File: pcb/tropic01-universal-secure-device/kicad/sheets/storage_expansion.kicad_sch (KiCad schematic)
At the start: 0 parts

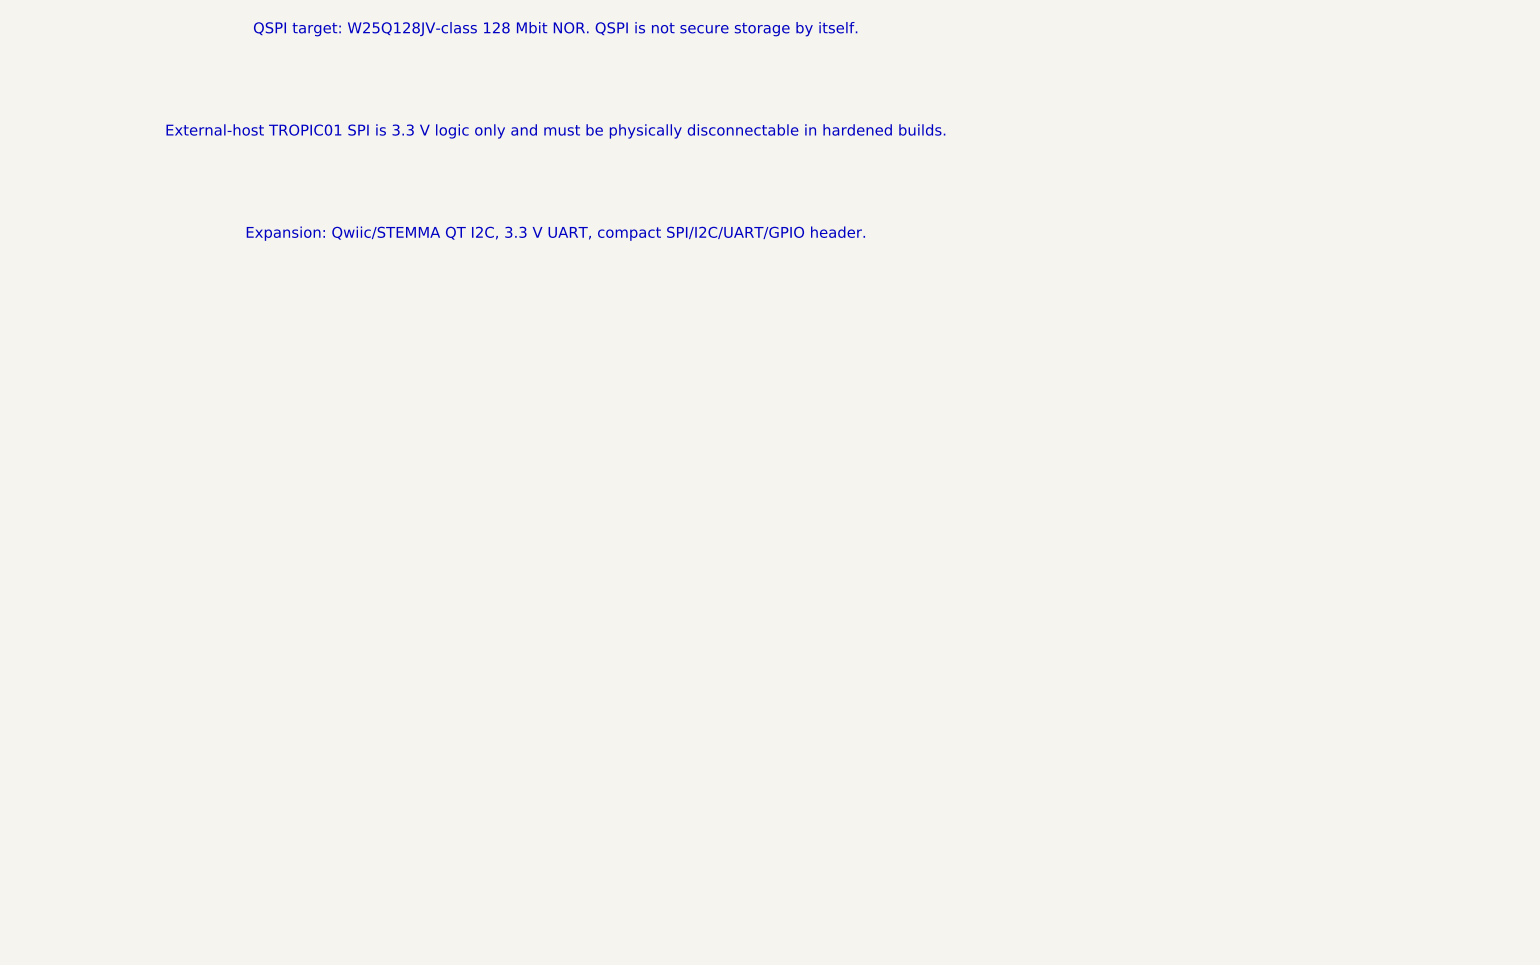
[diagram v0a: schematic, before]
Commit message: feat: materialize tropic01 schematic bindings
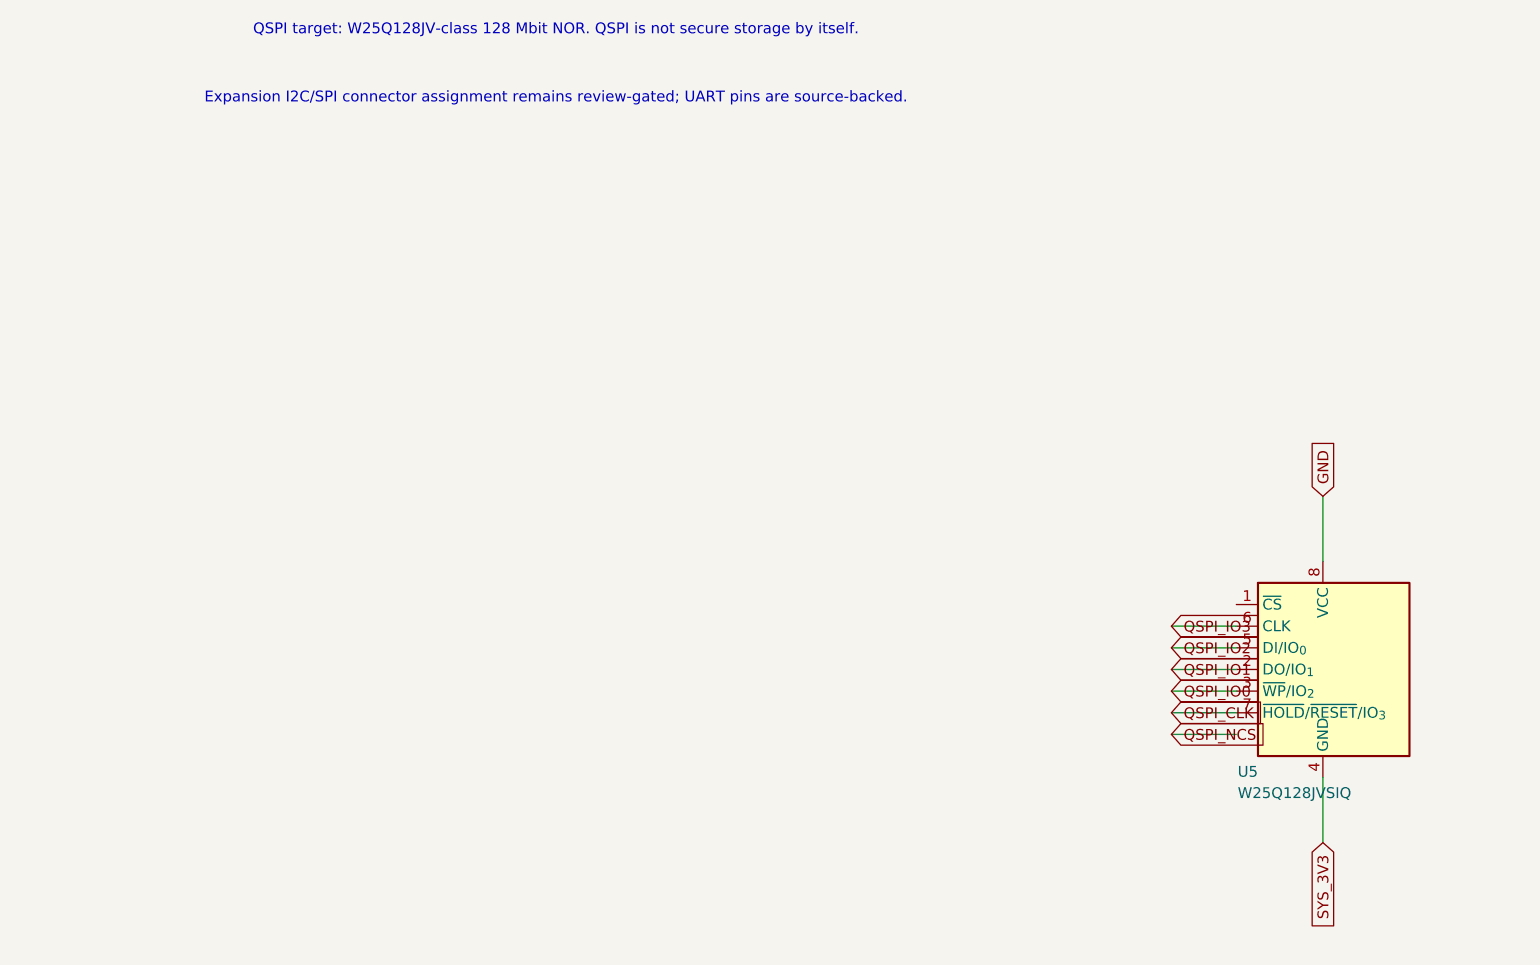
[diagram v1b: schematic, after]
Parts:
- added U5: W25Q128JVSIQ, Package_SO:SOIC-8_5.3x5.3mm_P1.27mm, symbol Memory_Flash:W25Q32JVSS
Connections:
- new net GND: U5.8 (VCC)
- new net QSPI_CLK: U5.7 (~{HOLD}/~{RESET}/IO_{3})
- new net QSPI_IO0: U5.3 (~{WP}/IO_{2})
- new net QSPI_IO1: U5.2 (DO/IO_{1})
- new net QSPI_IO2: U5.5 (DI/IO_{0})
- new net QSPI_IO3: U5.6 (CLK)
- new net SYS_3V3: U5.4 (GND)
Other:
- note added: "Expansion I2C/SPI connector assignment remains review-gated; UART pins are source-backed."
- note removed: "Expansion: Qwiic/STEMMA QT I2C, 3.3 V UART, compact SPI/I2C/UART/GPIO header."
- note removed: "External-host TROPIC01 SPI is 3.3 V logic only and must be physically disconnectable in hardened builds."
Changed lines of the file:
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@@
 	(text "QSPI target: W25Q128JV-class 128 Mbit NOR. QSPI is not secure storage by itself."
 		(exclude_from_sim no)
-		(at 20 20 0)
-		(effects
-			(font
-				(size 1.27 1.27)
+		(at 20.00 20.00 0)
+		(effects (font (size 1.27 1.27)))
+	)
+	(text "Expansion I2C/SPI connector assignment remains review-gated; UART pins are source-backed."
+		(exclude_from_sim no)
+		(at 20.00 28.00 0)
+		(effects (font (size 1.27 1.27)))
+	)
+	(symbol
+		(lib_id "Memory_Flash:W25Q32JVSS")
+		(at 110.00 95.00 0)
+		(unit 1)
+		(exclude_from_sim no)
+		(in_bom yes)
+		(on_board yes)
+		(dnp no)
+		(property "Reference" "U5"
+			(at 100.00 107.00 0)
+			(effects (font (size 1.27 1.27)) (justify left))
+		)
+		(property "Value" "W25Q128JVSIQ"
+			(at 100.00 109.50 0)
+			(effects (font (size 1.27 1.27)) (justify left))
+		)
+		(property "Footprint" "Package_SO:SOIC-8_5.3x5.3mm_P1.27mm"
+			(at 110.00 95.00 0)
+			(effects (font (size 1.27 1.27)) (hide yes))
+		)
+		(property "Datasheet" "https://www.winbond.com/resource-files/w25q128jv_dtr%20revc%2003272018%20plus.pdf"
+			(at 110.00 95.00 0)
+			(effects (font (size 1.27 1.27)) (hide yes))
+		)
+		(property "Description" "128 Mbit SPI/QSPI NOR flash using the KiCad W25Q32JVSS pin-compatible symbol"
+			(at 110.00 95.00 0)
+			(effects (font (size 1.27 1.27)) (hide yes))
+		)
+		(instances
+			(project "tropic01-universal-secure-device"
+				(path "/11111111-1111-4111-8111-111111111111/66666666-6666-4666-8666-666666666666"
+					(reference "U5")
+					(unit 1)
+				)
 			)
 		)
 	)
-	(text "External-host TROPIC01 SPI is 3.3 V logic only and must be physically disconnectable in hardened builds."
-		(exclude_from_sim no)
-		(at 20 32 0)
-		(effects
-			(font
-				(size 1.27 1.27)
-			)
+	(wire
+		(pts
+			(xy 99.84 102.62) (xy 92.22 102.62)
 		)
+		(stroke (width 0) (type default))
 	)
-	(text "Expansion: Qwiic/STEMMA QT I2C, 3.3 V UART, compact SPI/I2C/UART/GPIO header."
-		(exclude_from_sim no)
-		(at 20 44 0)
-		(effects
-			(font
-				(size 1.27 1.27)
-			)
+	(global_label "QSPI_NCS"
+		(shape input)
+		(at 92.22 102.62 0)
+		(fields_autoplaced)
+		(effects (font (size 1.27 1.27)))
+	)
+	(wire
+		(pts
+			(xy 99.84 95.00) (xy 92.22 95.00)
 		)
+		(stroke (width 0) (type default))
+	)
+	(global_label "QSPI_IO1"
+		(shape input)
+		(at 92.22 95.00 0)
+		(fields_autoplaced)
+		(effects (font (size 1.27 1.27)))
+	)
+	(wire
+		(pts
+			(xy 99.84 92.46) (xy 92.22 92.46)
+		)
+		(stroke (width 0) (type default))
+	)
+	(global_label "QSPI_IO2"
+		(shape input)
+		(at 92.22 92.46 0)
+		(fields_autoplaced)
+		(effects (font (size 1.27 1.27)))
+	)
+	(wire
+		(pts
+			(xy 110.00 82.30) (xy 110.00 74.68)
+		)
+		(stroke (width 0) (type default))
+	)
+	(global_label "GND"
+		(shape input)
+		(at 110.00 74.68 90)
+		(fields_autoplaced)
+		(effects (font (size 1.27 1.27)))
+	)
+	(wire
+		(pts
+			(xy 99.84 97.54) (xy 92.22 97.54)
+		)
+		(stroke (width 0) (type default))
+	)
+	(global_label "QSPI_IO0"
+		(shape input)
+		(at 92.22 97.54 0)
+		(fields_autoplaced)
+		(effects (font (size 1.27 1.27)))
+	)
+	(wire
+		(pts
+			(xy 99.84 100.08) (xy 92.22 100.08)
+		)
+		(stroke (width 0) (type default))
+	)
+	(global_label "QSPI_CLK"
+		(shape input)
+		(at 92.22 100.08 0)
+		(fields_autoplaced)
+		(effects (font (size 1.27 1.27)))
+	)
+	(wire
+		(pts
+			(xy 99.84 89.92) (xy 92.22 89.92)
+		)
+		(stroke (width 0) (type default))
+	)
+	(global_label "QSPI_IO3"
+		(shape input)
+		(at 92.22 89.92 0)
+		(fields_autoplaced)
+		(effects (font (size 1.27 1.27)))
+	)
+	(wire
+		(pts
+			(xy 110.00 107.70) (xy 110.00 115.32)
+		)
+		(stroke (width 0) (type default))
+	)
+	(global_label "SYS_3V3"
+		(shape input)
+		(at 110.00 115.32 270)
+		(fields_autoplaced)
+		(effects (font (size 1.27 1.27)))
 	)
 	(sheet_instances

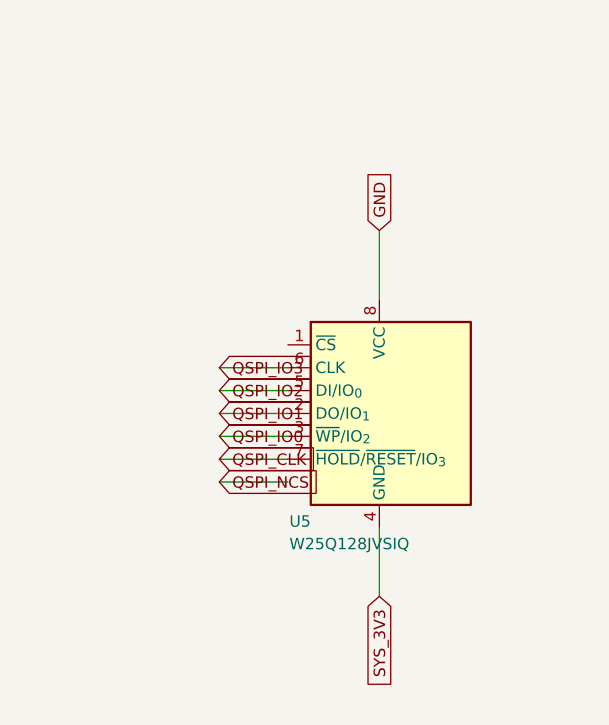
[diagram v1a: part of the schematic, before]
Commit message: feat: bind tropic01 pcb nets
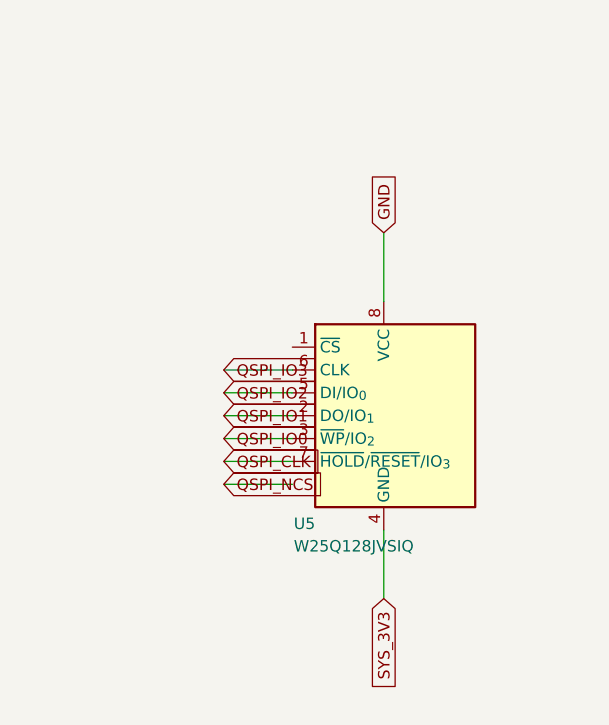
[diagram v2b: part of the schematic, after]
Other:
- moved on the sheet: U5
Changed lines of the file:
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@@
 	(symbol
 		(lib_id "Memory_Flash:W25Q32JVSS")
-		(at 110.00 95.00 0)
+		(at 110.49 95.25 0)
 		(unit 1)
 		(exclude_from_sim no)
@@
 		(dnp no)
 		(property "Reference" "U5"
-			(at 100.00 107.00 0)
+			(at 100.49 107.25 0)
 			(effects (font (size 1.27 1.27)) (justify left))
 		)
 		(property "Value" "W25Q128JVSIQ"
-			(at 100.00 109.50 0)
+			(at 100.49 109.75 0)
 			(effects (font (size 1.27 1.27)) (justify left))
 		)
 		(property "Footprint" "Package_SO:SOIC-8_5.3x5.3mm_P1.27mm"
-			(at 110.00 95.00 0)
+			(at 110.49 95.25 0)
 			(effects (font (size 1.27 1.27)) (hide yes))
 		)
 		(property "Datasheet" "https://www.winbond.com/resource-files/w25q128jv_dtr%20revc%2003272018%20plus.pdf"
-			(at 110.00 95.00 0)
+			(at 110.49 95.25 0)
 			(effects (font (size 1.27 1.27)) (hide yes))
 		)
 		(property "Description" "128 Mbit SPI/QSPI NOR flash using the KiCad W25Q32JVSS pin-compatible symbol"
-			(at 110.00 95.00 0)
+			(at 110.49 95.25 0)
 			(effects (font (size 1.27 1.27)) (hide yes))
 		)
@@
 	(wire
 		(pts
-			(xy 99.84 102.62) (xy 92.22 102.62)
+			(xy 100.33 102.87) (xy 92.71 102.87)
 		)
 		(stroke (width 0) (type default))
@@
 	(global_label "QSPI_NCS"
 		(shape input)
-		(at 92.22 102.62 0)
+		(at 92.71 102.87 0)
 		(fields_autoplaced)
 		(effects (font (size 1.27 1.27)))
@@
 	(wire
 		(pts
-			(xy 99.84 95.00) (xy 92.22 95.00)
+			(xy 100.33 95.25) (xy 92.71 95.25)
 		)
 		(stroke (width 0) (type default))
@@
 	(global_label "QSPI_IO1"
 		(shape input)
-		(at 92.22 95.00 0)
+		(at 92.71 95.25 0)
 		(fields_autoplaced)
 		(effects (font (size 1.27 1.27)))
@@
 	(wire
 		(pts
-			(xy 99.84 92.46) (xy 92.22 92.46)
+			(xy 100.33 92.71) (xy 92.71 92.71)
 		)
 		(stroke (width 0) (type default))
@@
 	(global_label "QSPI_IO2"
 		(shape input)
-		(at 92.22 92.46 0)
+		(at 92.71 92.71 0)
 		(fields_autoplaced)
 		(effects (font (size 1.27 1.27)))
@@
 	(wire
 		(pts
-			(xy 110.00 82.30) (xy 110.00 74.68)
+			(xy 110.49 82.55) (xy 110.49 74.93)
 		)
 		(stroke (width 0) (type default))
@@
 	(global_label "GND"
 		(shape input)
-		(at 110.00 74.68 90)
+		(at 110.49 74.93 90)
 		(fields_autoplaced)
 		(effects (font (size 1.27 1.27)))
@@
 	(wire
 		(pts
-			(xy 99.84 97.54) (xy 92.22 97.54)
+			(xy 100.33 97.79) (xy 92.71 97.79)
 		)
 		(stroke (width 0) (type default))
@@
 	(global_label "QSPI_IO0"
 		(shape input)
-		(at 92.22 97.54 0)
+		(at 92.71 97.79 0)
 		(fields_autoplaced)
 		(effects (font (size 1.27 1.27)))
@@
 	(wire
 		(pts
-			(xy 99.84 100.08) (xy 92.22 100.08)
+			(xy 100.33 100.33) (xy 92.71 100.33)
 		)
 		(stroke (width 0) (type default))
@@
 	(global_label "QSPI_CLK"
 		(shape input)
-		(at 92.22 100.08 0)
+		(at 92.71 100.33 0)
 		(fields_autoplaced)
 		(effects (font (size 1.27 1.27)))
@@
 	(wire
 		(pts
-			(xy 99.84 89.92) (xy 92.22 89.92)
+			(xy 100.33 90.17) (xy 92.71 90.17)
 		)
 		(stroke (width 0) (type default))
@@
 	(global_label "QSPI_IO3"
 		(shape input)
-		(at 92.22 89.92 0)
+		(at 92.71 90.17 0)
 		(fields_autoplaced)
 		(effects (font (size 1.27 1.27)))
@@
 	(wire
 		(pts
-			(xy 110.00 107.70) (xy 110.00 115.32)
+			(xy 110.49 107.95) (xy 110.49 115.57)
 		)
 		(stroke (width 0) (type default))
@@
 	(global_label "SYS_3V3"
 		(shape input)
-		(at 110.00 115.32 270)
+		(at 110.49 115.57 270)
 		(fields_autoplaced)
 		(effects (font (size 1.27 1.27)))
